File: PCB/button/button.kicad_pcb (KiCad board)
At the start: 2 copper layers, 40 x 46 mm, 23 parts, among them J1 Conn_01x02_Socket, J2 Conn_01x03_Socket, J3 Lamp Seat, J4 In, J5 Out, J6 Lamp Seat, J7 Lamp Seat, SW1 SW_SPST, U1 SS49E_SOT23

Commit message: Button PCB v1.0 rc3
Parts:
- removed J1: Conn_01x02_Socket, Connector_PinHeader_2.54mm:PinHeader_1x02_P2.54mm_Vertical
- added IR1: IR908-7C, button:IR908-7C, F.Cu at (89.5, 51.2)
- added JP3: c, button:SolderJump, B.Cu at (94.0, 54.0)
- added JP4: e, button:SolderJump, B.Cu at (94.0, 55.5)
- added JP5: sw1, button:SolderJump, B.Cu at (117.4, 52.3)
- added JP6: LEDP-V, button:SolderJump, B.Cu at (94.7, 47.5)
- added JP7: sw2, button:SolderJump, B.Cu at (82.6, 57.3)
- added PT1: PT908-7C, button:PT908-7C, F.Cu at (89.5, 58.8)
- added R3: 200, Resistor_SMD:R_0805_2012Metric_Pad1.20x1.40mm_HandSolder, B.Cu at (93.8, 51.0)
- added R4: 200, Resistor_SMD:R_0805_2012Metric, B.Cu at (85.0, 58.8)
- added R5: 200, Resistor_SMD:R_0805_2012Metric, B.Cu at (94.0, 58.8)
- added SW2: ~, button:SW_Kailh_Choc_V1V2, F.Cu at (88.5, 55.0)
- added Z1: 3.3V, Diode_SMD:D_SOD-123F, B.Cu at (109.0, 63.0)
- J2: footprint Connector_PinHeader_2.54mm:PinHeader_1x03_P2.54mm_Vertical -> button:SH1.0_3P_Solder_Combo
- J4: value In -> RGB In; footprint Connector_PinHeader_2.54mm:PinHeader_1x03_P2.54mm_Vertical -> button:SH1.0_3P_Solder_Combo
- J5: value Out -> RGB Out; footprint Connector_PinHeader_2.54mm:PinHeader_1x03_P2.54mm_Vertical -> button:SH1.0_3P_Solder_Combo
- SW1: value SW_SPST -> ~
- moved J2 32.9 mm to (116.5, 46.0), turned to -90 degrees
- moved S3 2.12 mm to (91.5, 44.5)
- moved S4 2.12 mm to (91.5, 65.5)
- moved J6 2.00 mm to (110.5, 36.0)
- moved J7 2.00 mm to (110.5, 74.0)
- moved J4 1.52 mm to (100.0, 45.5), turned to 0 degrees
- moved J5 1.43 mm to (100.0, 64.5), turned to 180 degrees
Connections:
- SW1 pad 1: /Out -> Net-(JP5-A)
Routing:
- net Vcc: track 38.5 -> 71.6 mm, vias 0 -> 3
- net /Out: track 43.3 -> 74.7 mm, vias 1 -> 2
- net Net-(JP3-B): track 0.00 -> 10.2 mm
- net GND: track 34.4 -> 26.0 mm, vias 7 -> 19
- net LED_P: track 183.6 -> 175.5 mm, vias 3 -> 5
- net Net-(JP4-B): track 0.00 -> 5.38 mm
- net LED_N: track 170.7 -> 174.0 mm, vias 2 -> 3
- net Net-(IR1-A): track 0.00 -> 2.11 mm
- net Net-(JP5-A): track 0.00 -> 2.05 mm
- net Net-(D4-Out): track 29.6 -> 31.6 mm
- net Net-(D3-In): track 37.4 -> 39.4 mm
- net Net-(JP7-A): track 0.00 -> 1.67 mm
- net Net-(J3-In): track 12.7 -> 14.2 mm
- net Net-(J3-Out): track 15.0 -> 14.5 mm
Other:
- outline, holes or cut-outs redrawn
- board text added: "-~+"
- board text added: "LED In"
- board text added: "LED Out"
- board text added: "SW"
- board text added: "V Out G"
- board text removed: "+ in -"
- board text removed: "+ out -"
- board text removed: "G Out V"

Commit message: Button and IO8 PCB
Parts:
- removed IR1: IR908-7C, button:IR908-7C
- removed PT1: PT908-7C, button:PT908-7C
- J6, J7: value Lamp Seat -> Gold Finger
- SW2: value ~ -> Choc and IR Pair; footprint button:SW_Kailh_Choc_V1V2 -> button:SW_Kailh_Choc_IR_Combo
- moved J6 3.50 mm to (114.0, 36.0)
- moved J7 3.50 mm to (114.0, 74.0)
- turned Z1 to 0 degrees
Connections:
- R3 pad 1: Net-(IR1-A) -> Net-(SW2B-A)
- Z1 pad 1: GND -> /Out
- Z1 pad 2: /Out -> GND
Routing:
- net LED_P: track 175.5 -> 184.4 mm
- net LED_N: track 174.0 -> 181.0 mm
- net Net-(D3-In): track 39.4 -> 42.9 mm
- net Net-(D4-Out): track 31.6 -> 35.1 mm
- net GND: track 26.0 -> 23.5 mm
- net Net-(IR1-A): track 2.11 -> 0.00 mm
- net Net-(SW2B-A): track 0.00 -> 2.11 mm
- net Net-(JP3-B): track 10.2 -> 12.2 mm
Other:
- outline, holes or cut-outs redrawn

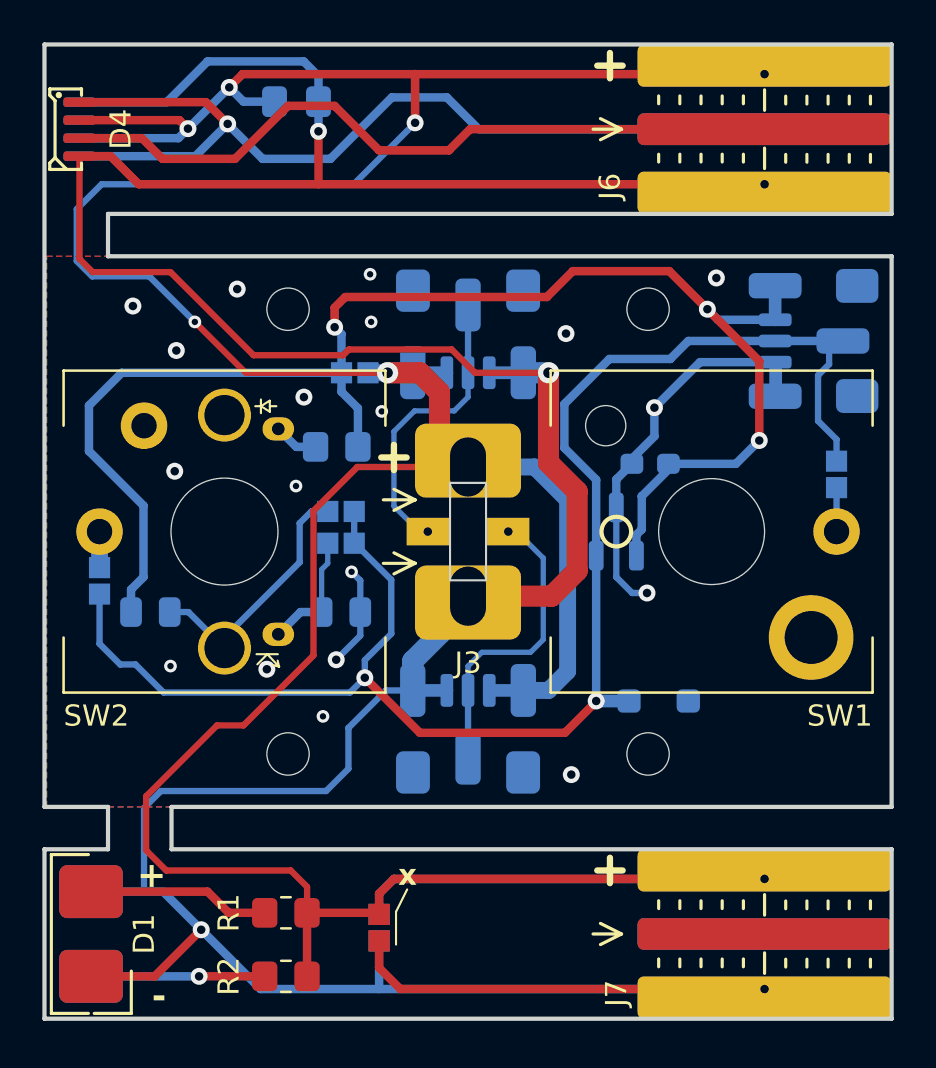
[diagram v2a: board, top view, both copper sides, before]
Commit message: Better screw clearance
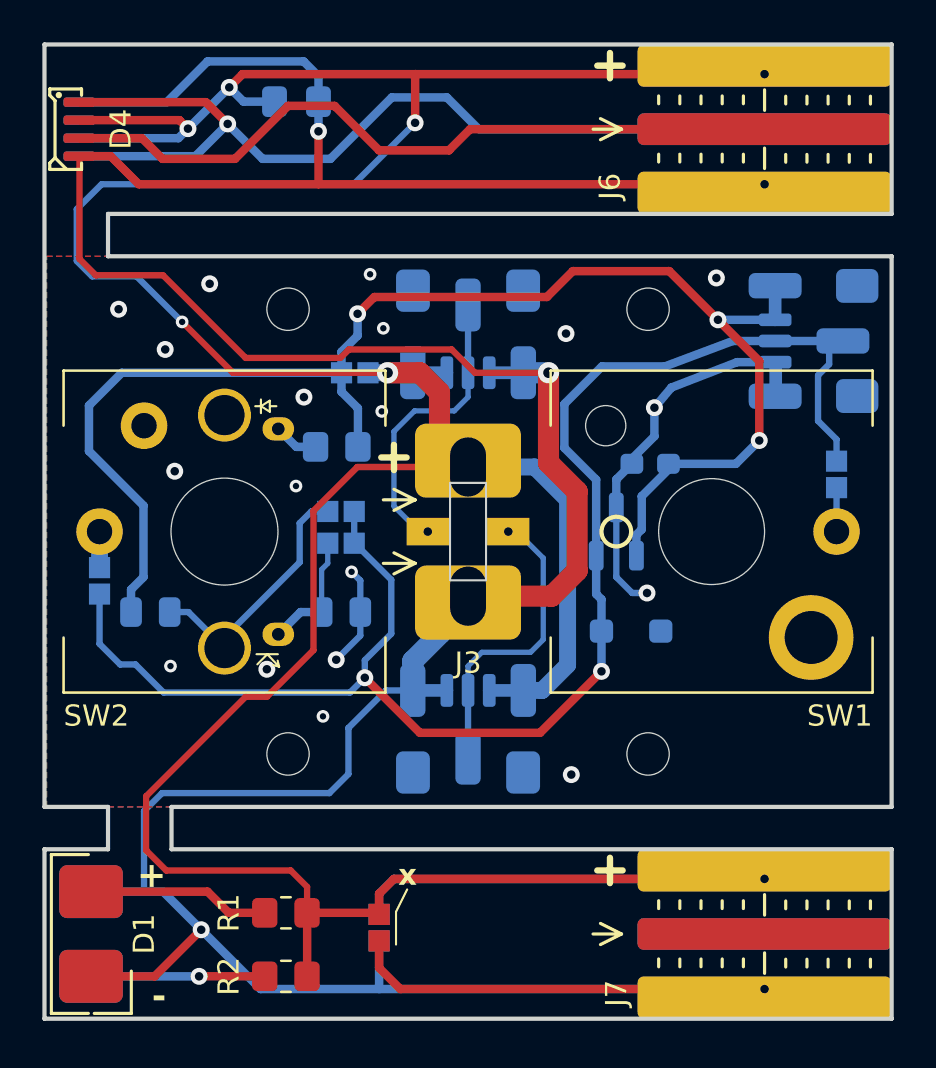
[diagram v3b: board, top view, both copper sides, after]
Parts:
- moved Z1 3.55 mm to (107.7, 59.7)
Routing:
- net /Out: track 74.7 -> 72.4 mm
- net Vcc: track 71.6 -> 69.8 mm
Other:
- board text added: "Arcade Pico Button v1.01"
- board text removed: "Arcade Pico Button v1.0"
